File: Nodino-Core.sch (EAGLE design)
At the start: 15 parts, among them CON1 NODINO-JTAGMODULE, CON2 USB-OTG_SHIELD, IC1 STM32F373CCT6, IC3 AP733333SAG, Q1 16MHz, Y1 32.768kHz

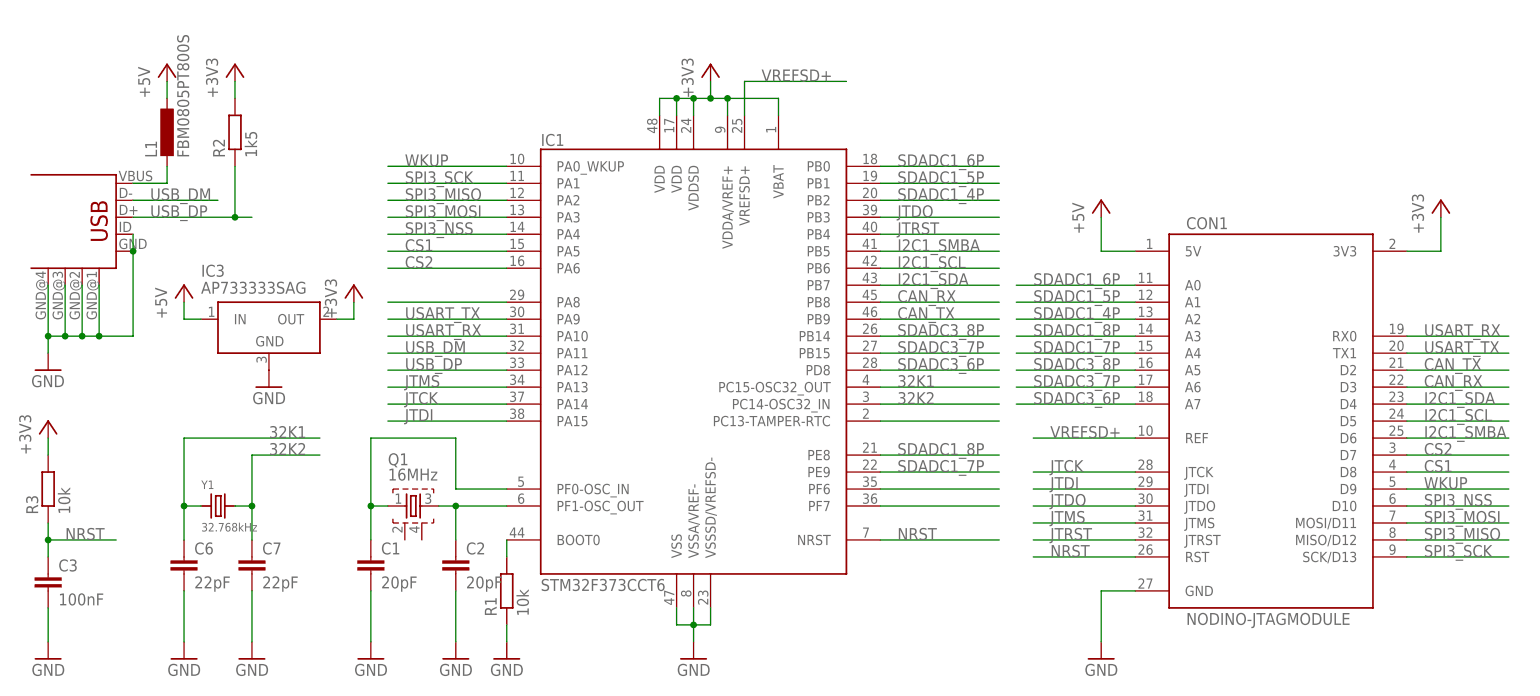
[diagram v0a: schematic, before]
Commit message: Name and value renumbering
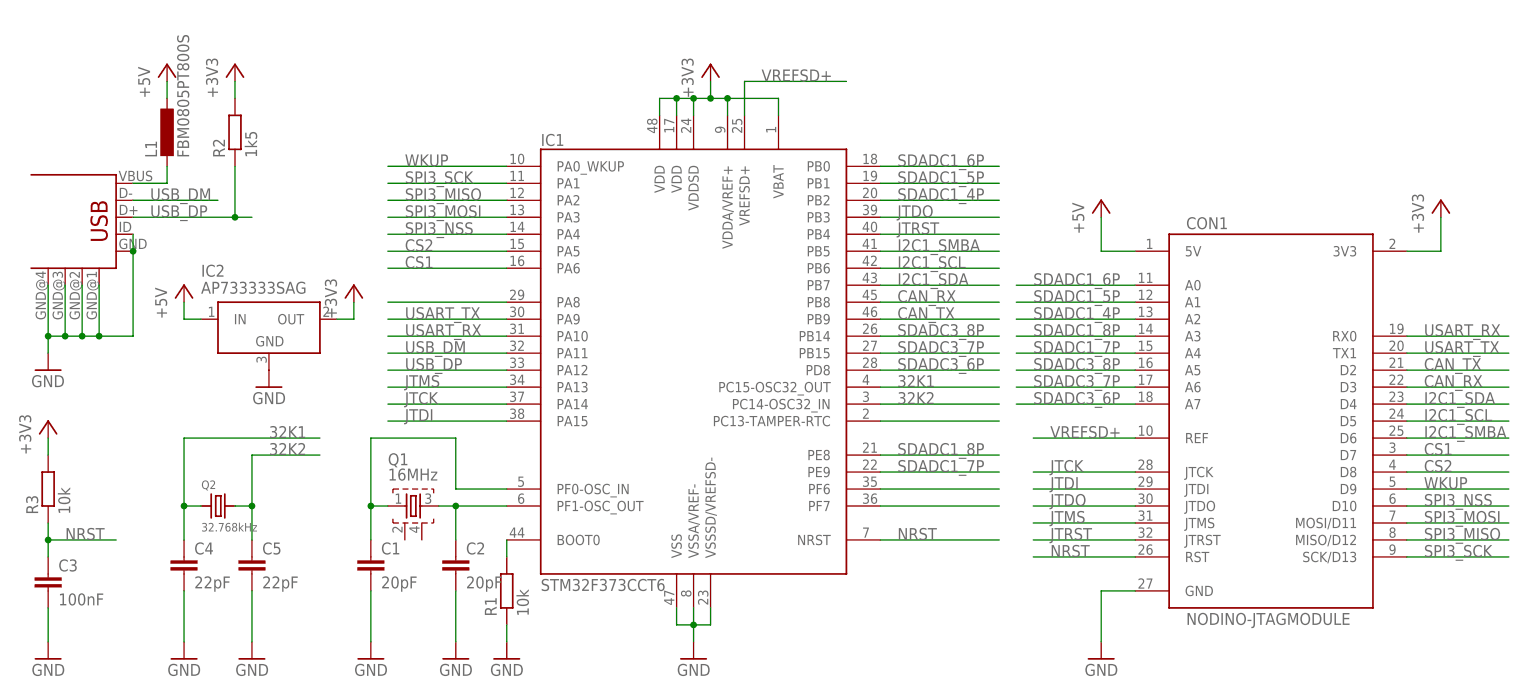
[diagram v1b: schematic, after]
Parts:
- renumbered C6 to C4, C7 to C5, IC3 to IC2, Y1 to Q2
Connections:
- net CS1: now also CON1.D7, IC1.PA6; no longer CON1.D8, IC1.PA5
- net CS2: now also CON1.D8, IC1.PA5; no longer CON1.D7, IC1.PA6
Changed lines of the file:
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@@
 <part name="+3V2" library="supply1" deviceset="+3V3" device=""/>
 <part name="GND1" library="supply1" deviceset="GND" device=""/>
-<part name="C6" library="resistor" deviceset="C-EU" device="C0603K" value="22pF"/>
-<part name="C7" library="resistor" deviceset="C-EU" device="C0603K" value="22pF"/>
+<part name="C4" library="resistor" deviceset="C-EU" device="C0603K" value="22pF"/>
+<part name="C5" library="resistor" deviceset="C-EU" device="C0603K" value="22pF"/>
 <part name="GND12" library="supply1" deviceset="GND" device=""/>
 <part name="GND13" library="supply1" deviceset="GND" device=""/>
-<part name="Y1" library="abracon" deviceset="CRYSTAL" device=".ABS07" value="32.768kHz"/>
-<part name="IC3" library="diodes_inc" deviceset="AP7333" device="33SAG"/>
+<part name="Q2" library="abracon" deviceset="CRYSTAL" device=".ABS07" value="32.768kHz"/>
+<part name="IC2" library="diodes_inc" deviceset="AP7333" device="33SAG"/>
 <part name="P+3" library="supply1" deviceset="+5V" device=""/>
 <part name="+3V6" library="supply1" deviceset="+3V3" device=""/>
@@
 <instance part="+3V2" gate="G$1" x="210.82" y="76.2"/>
 <instance part="GND1" gate="1" x="160.02" y="7.62" rot="MR0"/>
-<instance part="C6" gate="G$1" x="22.86" y="22.86"/>
-<instance part="C7" gate="G$1" x="33.02" y="22.86"/>
+<instance part="C4" gate="G$1" x="22.86" y="22.86"/>
+<instance part="C5" gate="G$1" x="33.02" y="22.86"/>
 <instance part="GND12" gate="1" x="22.86" y="7.62" rot="MR0"/>
 <instance part="GND13" gate="1" x="33.02" y="7.62" rot="MR0"/>
-<instance part="Y1" gate="G$1" x="27.94" y="30.48"/>
-<instance part="IC3" gate="G$1" x="35.56" y="55.88" smashed="yes">
+<instance part="Q2" gate="G$1" x="27.94" y="30.48"/>
+<instance part="IC2" gate="G$1" x="35.56" y="55.88" smashed="yes">
 <attribute name="NAME" x="25.4" y="64.77" size="1.778" layer="95"/>
 <attribute name="VALUE" x="25.4" y="62.23" size="1.778" layer="96"/>
@@
 </segment>
 <segment>
-<pinref part="C6" gate="G$1" pin="2"/>
+<pinref part="C4" gate="G$1" pin="2"/>
 <pinref part="GND12" gate="1" pin="GND"/>
 <wire x1="22.86" y1="17.78" x2="22.86" y2="10.16" width="0.1524" layer="91"/>
 </segment>
 <segment>
-<pinref part="C7" gate="G$1" pin="2"/>
+<pinref part="C5" gate="G$1" pin="2"/>
 <pinref part="GND13" gate="1" pin="GND"/>
 <wire x1="33.02" y1="17.78" x2="33.02" y2="10.16" width="0.1524" layer="91"/>
 </segment>
 <segment>
-<pinref part="IC3" gate="G$1" pin="GND"/>
+<pinref part="IC2" gate="G$1" pin="GND"/>
 <pinref part="GND11" gate="1" pin="GND"/>
 </segment>
@@
 </segment>
 <segment>
-<pinref part="IC3" gate="G$1" pin="OUT"/>
+<pinref part="IC2" gate="G$1" pin="OUT"/>
 <pinref part="+3V6" gate="G$1" pin="+3V3"/>
 <wire x1="45.72" y1="58.42" x2="48.26" y2="58.42" width="0.1524" layer="91"/>
@@
 </segment>
 </net>
-<net name="CS1" class="0">
+<net name="CS2" class="0">
 <segment>
 <pinref part="IC1" gate="G$1" pin="PA5"/>
@@
 </segment>
 </net>
-<net name="CS2" class="0">
+<net name="CS1" class="0">
 <segment>
 <pinref part="IC1" gate="G$1" pin="PA6"/>
@@
 <pinref part="P+3" gate="1" pin="+5V"/>
 <wire x1="22.86" y1="60.96" x2="22.86" y2="58.42" width="0.1524" layer="91"/>
-<pinref part="IC3" gate="G$1" pin="IN"/>
+<pinref part="IC2" gate="G$1" pin="IN"/>
 <wire x1="22.86" y1="58.42" x2="25.4" y2="58.42" width="0.1524" layer="91"/>
 </segment>
@@
 <net name="32K1" class="0">
 <segment>
-<pinref part="C6" gate="G$1" pin="1"/>
+<pinref part="C4" gate="G$1" pin="1"/>
 <wire x1="25.4" y1="30.48" x2="22.86" y2="30.48" width="0.1524" layer="91"/>
 <wire x1="22.86" y1="30.48" x2="22.86" y2="25.4" width="0.1524" layer="91"/>
-<pinref part="Y1" gate="G$1" pin="1"/>
+<pinref part="Q2" gate="G$1" pin="1"/>
 <wire x1="43.18" y1="40.64" x2="22.86" y2="40.64" width="0.1524" layer="91"/>
 <wire x1="22.86" y1="40.64" x2="22.86" y2="30.48" width="0.1524" layer="91"/>
@@
 <net name="32K2" class="0">
 <segment>
-<pinref part="C7" gate="G$1" pin="1"/>
+<pinref part="C5" gate="G$1" pin="1"/>
 <wire x1="30.48" y1="30.48" x2="33.02" y2="30.48" width="0.1524" layer="91"/>
 <wire x1="33.02" y1="30.48" x2="33.02" y2="25.4" width="0.1524" layer="91"/>
-<pinref part="Y1" gate="G$1" pin="2"/>
+<pinref part="Q2" gate="G$1" pin="2"/>
 <wire x1="43.18" y1="38.1" x2="33.02" y2="38.1" width="0.1524" layer="91"/>
 <wire x1="33.02" y1="38.1" x2="33.02" y2="30.48" width="0.1524" layer="91"/>
